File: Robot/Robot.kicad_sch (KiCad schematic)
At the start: 33 parts, among them J1 Barrel_Jack, J10 Conn_01x03_Pin, J11 Stepper_2, J2 Conn_01x02_Pin, J3 Stepper_2, J4 UltraSonic, J5 MotorController, J6 Range, J7 Conn_01x04_Pin, J8 Conn_01x03_Pin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

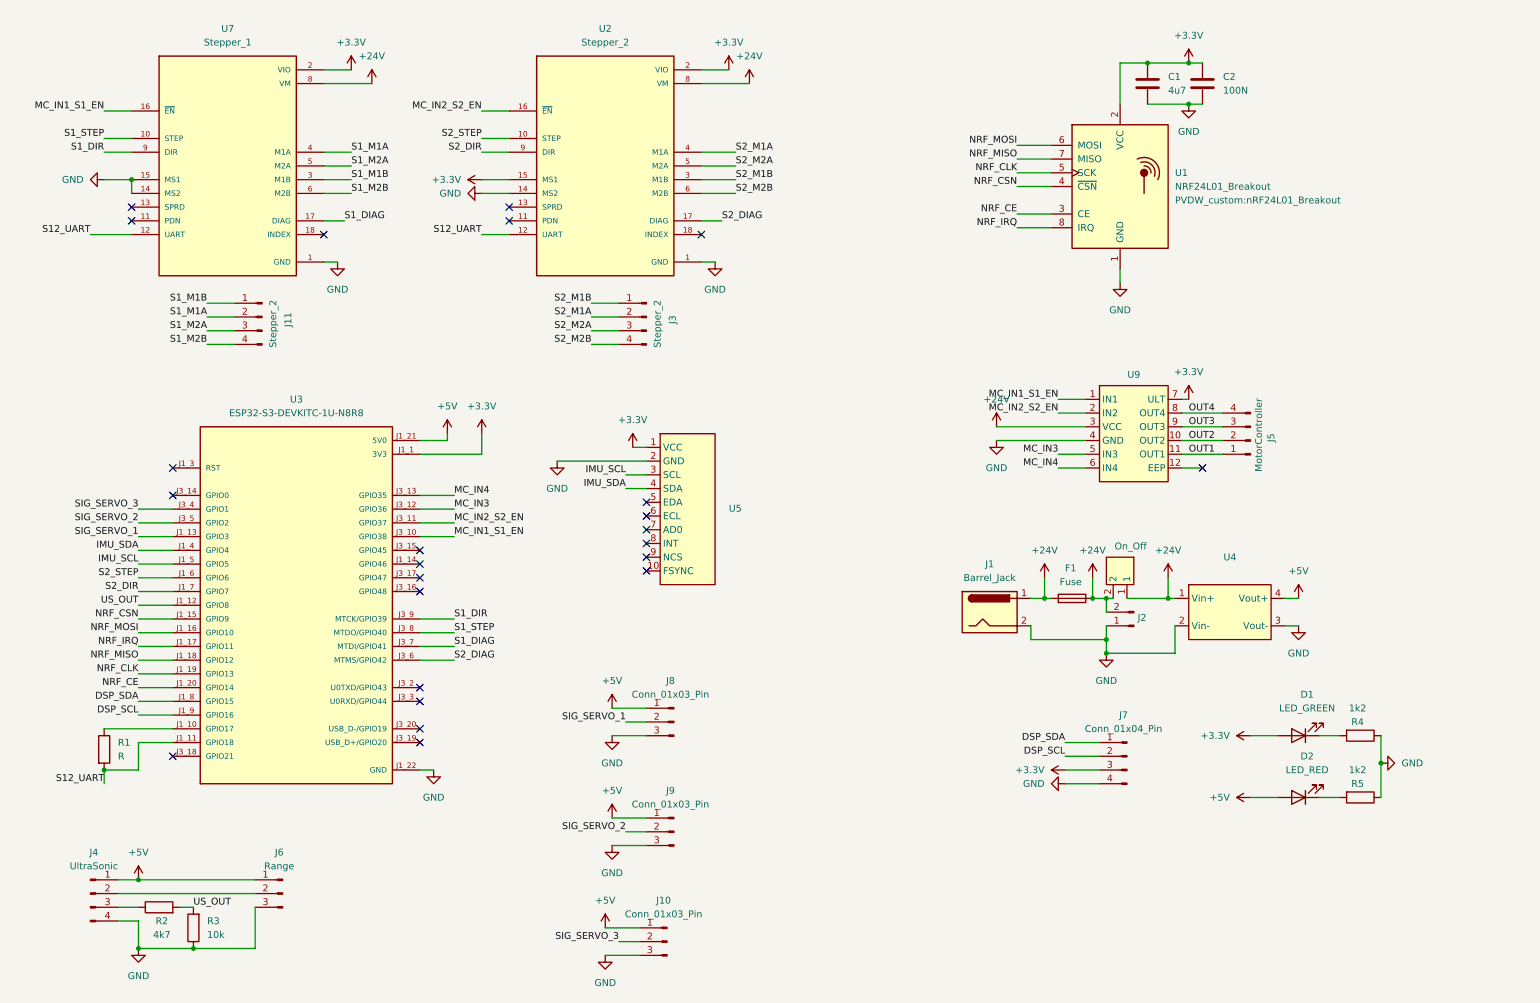
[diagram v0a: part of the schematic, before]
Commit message: Updated robot and created 0402 test pcb
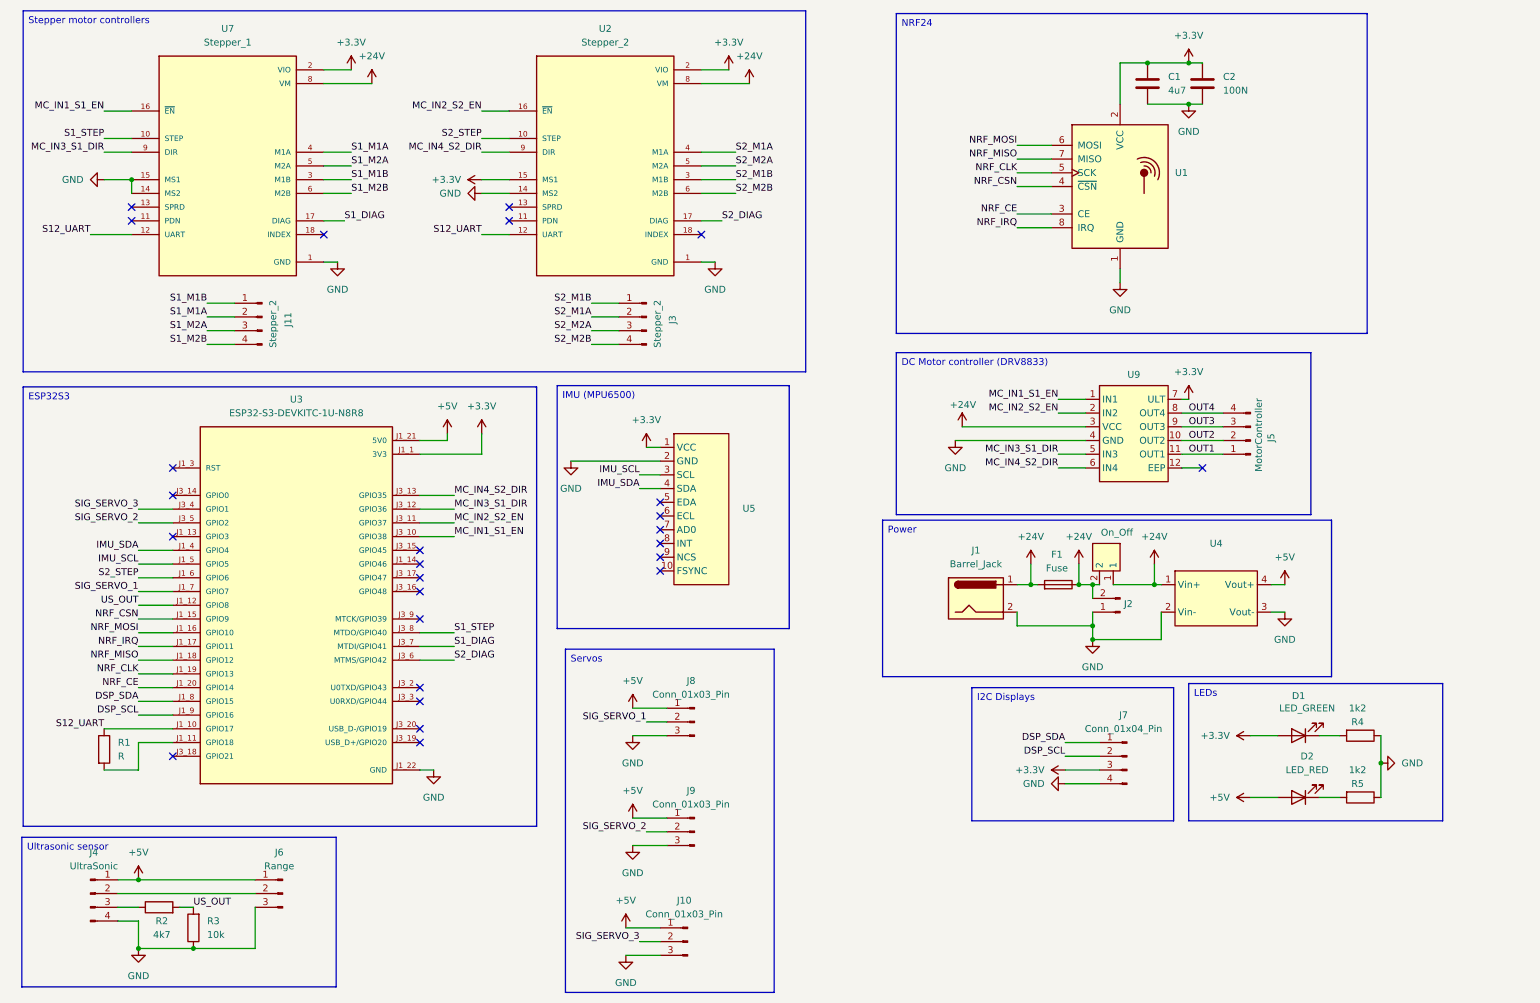
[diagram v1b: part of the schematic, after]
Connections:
- net S12_UART: now also R1.1, U3.J1_10 (GPIO17); no longer R1.2, U3.J1_11 (GPIO18)
- net SIG_SERVO_1: now also U3.J1_7 (GPIO7); no longer U3.J1_13 (GPIO3)
- net MC_IN3 renamed MC_IN3_S1_DIR
- net MC_IN3_S1_DIR: now also U7.9 (DIR)
- net MC_IN4 renamed MC_IN4_S2_DIR
- net MC_IN4_S2_DIR: now also U2.9 (DIR)
- net S1_DIR: no longer names the net of U3.J3_9 (MTCK/GPIO39)
- net S1_DIR: no longer U7.9 (DIR)
- removed net S2_DIR: U2.9 (DIR), U3.J1_7 (GPIO7)
- new net: R1.2, U3.J1_11 (GPIO18)
- no-connect marks 24 -> 26
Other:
- title: (none) -> Self balancing robot
- moved on the sheet: F1, J1, J10, J2, J8, J9, U4, U5

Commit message: New versions for Robot PCBs
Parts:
- removed R2: 4k7, Resistor_SMD:R_0805_2012Metric_Pad1.20x1.40mm_HandSolder, symbol Device:R
- removed R3: 10k, Resistor_SMD:R_0805_2012Metric_Pad1.20x1.40mm_HandSolder, symbol Device:R
- J2, U8: footprint PVDW_custom:Connector_1x2_p2.54_vertical -> PVDW_custom:screw_block_2pin
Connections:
- net +3.3V: now also J4.1 (Pin_1), J6.1 (Pin_1), U9.12 (EEP); no longer U9.7 (ULT)
- net +5V: now also J10.3 (Pin_3), J8.3 (Pin_3), J9.3 (Pin_3); no longer J10.1 (Pin_1), J4.1 (Pin_1), J6.1 (Pin_1), J8.1 (Pin_1), J9.1 (Pin_1)
- net GND: now also J10.1 (Pin_1), J8.1 (Pin_1), J9.1 (Pin_1), U9.3 (GND); no longer J10.3 (Pin_3), J8.3 (Pin_3), J9.3 (Pin_3), U9.4 (GND)
- net S12_UART: now also U2.11 (PDN), U7.11 (PDN); no longer U2.12 (UART), U7.12 (UART)
- net US_OUT: now also J4.3 (Pin_3)
- net UART_TX: now reaches R1.2, U3.J1_11 (GPIO18)
- net IMU_INT: now reaches U5.8 (INT)
- net IMU_INT: now also U3.J1_13 (GPIO3)
- removed net +24V: F1.1, F1.2, J1.1, J2.2 (Pin_2), U2.8 (VM), U4.1 (Vin+), U7.8 (VM), U8.1, U8.2, U9.3 (VCC)
- new net VBat: F1.1, J1.1, J2.2 (Pin_2)
- new net VDC: U2.8 (VM), U4.1 (Vin+), U7.8 (VM), U8.1, U9.4 (VCC)
- new net Vin: F1.2, U8.2
- no-connect marks 26 -> 24
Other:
- moved on the sheet: H1, H2, H3, H4, J2

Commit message: Fixed VCC-GND mixup on drv8833
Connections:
- net GND: now also U9.4 (GND); no longer U9.3 (GND)
- net VDC: now also U9.3 (VCC); no longer U9.4 (VCC)
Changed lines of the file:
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@@
 	(symbol
 		(lib_id "power:GND")
-		(at 187.96 91.44 180)
+		(at 186.69 93.98 0)
 		(unit 1)
 		(exclude_from_sim no)
@@
 		(dnp no)
 		(property "Reference" "#PWR016"
-			(at 187.96 85.09 0)
+			(at 186.69 100.33 0)
 			(effects
 				(font
@@
 		)
 		(property "Value" "GND"
-			(at 187.96 86.36 0)
+			(at 186.69 99.06 0)
 			(effects
 				(font
@@
 		)
 		(property "Footprint" ""
-			(at 187.96 91.44 0)
+			(at 186.69 93.98 0)
 			(effects
 				(font
@@
 		)
 		(property "Datasheet" ""
-			(at 187.96 91.44 0)
+			(at 186.69 93.98 0)
 			(effects
 				(font
@@
 		)
 		(property "Description" "Power symbol creates a global label with name \"GND\" , ground"
-			(at 187.96 91.44 0)
+			(at 186.69 93.98 0)
 			(effects
 				(font
@@
 	(symbol
 		(lib_id "power:+24V")
-		(at 186.69 93.98 180)
+		(at 187.96 91.44 0)
 		(unit 1)
 		(exclude_from_sim no)
@@
 		(dnp no)
 		(property "Reference" "#PWR015"
-			(at 186.69 90.17 0)
+			(at 187.96 95.25 0)
 			(effects
 				(font
@@
 		)
 		(property "Value" "VDC"
-			(at 188.976 98.044 0)
+			(at 185.674 87.376 0)
 			(effects
 				(font
@@
 		)
 		(property "Footprint" ""
-			(at 186.69 93.98 0)
+			(at 187.96 91.44 0)
 			(effects
 				(font
@@
 		)
 		(property "Datasheet" ""
-			(at 186.69 93.98 0)
+			(at 187.96 91.44 0)
 			(effects
 				(font
@@
 		)
 		(property "Description" "Power symbol creates a global label with name \"+24V\""
-			(at 186.69 93.98 0)
-			(effects
-				(font
+			(at 187.96 91.44 0)
+			(effects
+				(font

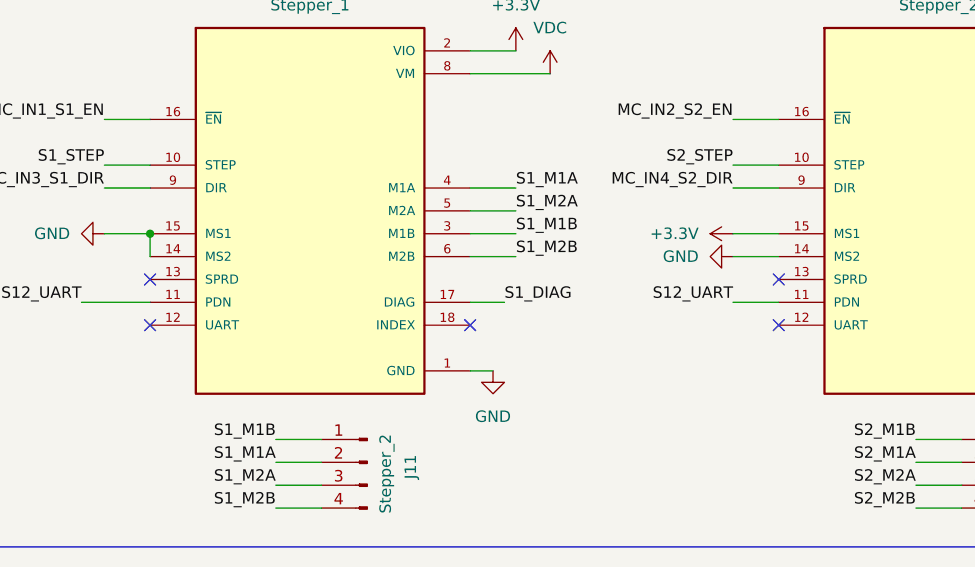
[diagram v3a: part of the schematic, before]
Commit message: Minor bugfixes in Robot PCB (UART connected to the wrong pin of the stepper driver)
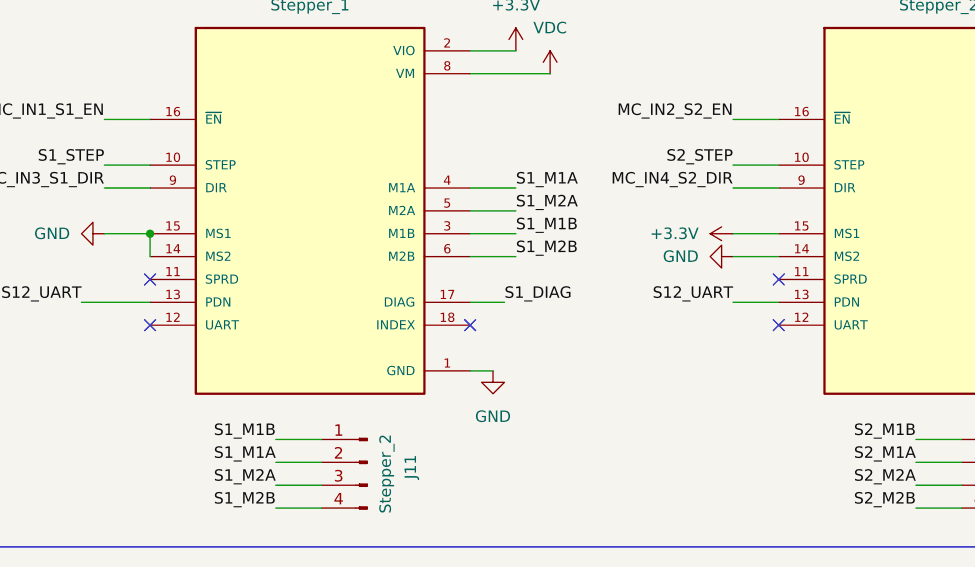
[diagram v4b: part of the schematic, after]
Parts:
- U4, U5, U9: value ~ -> (none)
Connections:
- net S12_UART: now also U2.13 (PDN), U7.13 (PDN); no longer U2.11 (PDN), U7.11 (PDN)

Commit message: New PCB Layout for Robot
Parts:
- removed C1: 4u7, Capacitor_SMD:C_0805_2012Metric_Pad1.18x1.45mm_HandSolder, symbol Device:C
- removed C2: 100N, Capacitor_SMD:C_0805_2012Metric_Pad1.18x1.45mm_HandSolder, symbol Device:C
- removed D1: LED_GREEN, LED_SMD:LED_0805_2012Metric_Pad1.15x1.40mm_HandSolder, symbol Device:LED
- removed D2: LED_RED, LED_SMD:LED_0805_2012Metric_Pad1.15x1.40mm_HandSolder, symbol Device:LED
- removed F1: Fuse, PVDW_custom:FUSE_3544-2, symbol PVDW_custom:Fuse
- removed J1: Barrel_Jack, PVDW_custom:DC_Jack_PCB, symbol PVDW_custom:Barrel_Jack
- removed J10, J8, J9: Conn_01x03_Pin, PVDW_custom:3PIN_SERVO, symbol Connector:Conn_01x03_Pin
- removed J2: Conn_01x02_Pin, PVDW_custom:screw_block_2pin, symbol Connector:Conn_01x02_Pin
- removed J4: UltraSonic, PVDW_custom:Connector_1x4_p2.54_vertical_stepper, symbol PVDW_custom:Conn_01x04_Pin
- removed J5: MotorController, PVDW_custom:Connector_1x4_p2.54_vertical_stepper, symbol PVDW_custom:Conn_01x04_Pin
- removed J6: Range, Connector_PinHeader_2.54mm:PinHeader_1x03_P2.54mm_Vertical, symbol Connector:Conn_01x03_Pin
- removed J7: Conn_01x04_Pin, PVDW_custom:Connector_1x4_p2.54_vertical_stepper, symbol PVDW_custom:Conn_01x04_Pin
- removed R4, R5: 1k2, Resistor_SMD:R_0805_2012Metric_Pad1.20x1.40mm_HandSolder, symbol Device:R
- removed U1: NRF24L01_Breakout, PVDW_custom:nRF24L01_Breakout, symbol PVDW_custom:NRF24L01_Breakout
- removed U8: On_Off, PVDW_custom:screw_block_2pin, symbol PVDW_custom:2Pin_generic
- removed U9: (no value), PVDW_custom:DRV8833, symbol PVDW_custom:drv8833_board
- added J1: Conn_01x02_Pin, Connector_AMASS:AMASS_XT60PW-M_1x02_P7.20mm_Horizontal, symbol Connector:Conn_01x02_Pin
- added J2: Dsp1, PVDW_custom:PinHeader_max7219, symbol Connector:Conn_01x05_Pin
- added J4: Dsp2, PVDW_custom:PinHeader_max7219, symbol Connector:Conn_01x05_Pin
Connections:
- net SIG_SERVO_2 is gone; now on net S2_STEP: U3.J3_5 (GPIO2)
- net +5V: now also J2.1 (Pin_1), J4.1 (Pin_1)
- net GND: now also J1.2 (Pin_2), J2.2 (Pin_2), J4.2 (Pin_2)
- net IMU_INT: now also U3.J1_4 (GPIO4); no longer U3.J1_13 (GPIO3)
- net IMU_SCL: now also U3.J1_6 (GPIO6); no longer U3.J1_5 (GPIO5)
- net IMU_SDA: now also U3.J1_5 (GPIO5); no longer U3.J1_4 (GPIO4)
- net S1_STEP: now also U3.J3_15 (GPIO45); no longer U3.J3_8 (MTDO/GPIO40)
- net S2_DIAG: now also U3.J3_3 (U0RXD/GPIO44); no longer U3.J3_6 (MTMS/GPIO42)
- net S2_STEP: no longer U3.J1_6 (GPIO6)
- net VDC: now also J1.1 (Pin_1)
- net S1_DIR: now reaches U3.J3_16 (GPIO48)
- net S1_DIR: now also U7.9 (DIR)
- net DSP_SCL: no longer names the net of U3.J1_9 (GPIO16)
- net DSP_SDA: no longer names the net of U3.J1_8 (GPIO15)
- net MC_IN1_S1_EN renamed S1_EN
- net MC_IN2_S2_EN: no longer names the net of U3.J3_11 (GPIO37)
- net MC_IN2_S2_EN: no longer U2.16 (~{EN})
- net MC_IN3_S1_DIR: no longer names the net of U3.J3_12 (GPIO36)
- net MC_IN3_S1_DIR: no longer U7.9 (DIR)
- net MC_IN4_S2_DIR: no longer names the net of U3.J3_13 (GPIO35)
- net MC_IN4_S2_DIR: no longer U2.9 (DIR)
- net NRF_CE: no longer names the net of U3.J1_20 (GPIO14)
- net NRF_CLK renamed CS
- net CS: now also J2.4 (Pin_4), J4.4 (Pin_4)
- net NRF_CSN renamed MOSI
- net MOSI: now also J2.3 (Pin_3)
- net NRF_IRQ: no longer names the net of U3.J1_17 (GPIO11)
- net NRF_MISO: no longer names the net of U3.J1_18 (GPIO12)
- net NRF_MOSI renamed CLK
- net CLK: now also J2.5 (Pin_5), J4.5 (Pin_5)
- net SIG_SERVO_1: no longer names the net of U3.J1_7 (GPIO7)
- net SIG_SERVO_3 renamed S2_EN
- net S2_EN: now also U2.16 (~{EN})
- new net S2_DIR: U2.9 (DIR), U3.J3_6 (MTMS/GPIO42)
- no-connect marks 24 -> 28

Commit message: New version
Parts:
- removed J4: Dsp2, PVDW_custom:PinHeader_max7219, symbol Connector:Conn_01x05_Pin
- removed U4: (no value), PVDW_custom:LM1584EN, symbol PVDW_custom:LM1584EN
- added C1, C2: C_Polarized, Capacitor_THT:C_Radial_D10.0mm_H20.0mm_P5.00mm, symbol Device:C_Polarized
- added J4: Conn_01x02_Pin, Connector_PinHeader_2.54mm:PinHeader_1x02_P2.54mm_Vertical, symbol Connector:Conn_01x02_Pin
- added U1: LM7805_TO220, Package_TO_SOT_THT:TO-220-3_Vertical, symbol Regulator_Linear:LM7805_TO220
- J1: footprint Connector_AMASS:AMASS_XT60PW-M_1x02_P7.20mm_Horizontal -> Connector_AMASS:AMASS_XT60-F_1x02_P7.20mm_Vertical
- J2: footprint PVDW_custom:PinHeader_max7219 -> Connector_PinHeader_2.54mm:PinHeader_1x05_P2.54mm_Vertical
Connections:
- net +5V: now also C1.1, U1.3 (VO)
- net GND: now also J1.1 (Pin_1), C1.2, C2.2, J4.2 (Pin_2), U1.2 (GND); no longer J1.2 (Pin_2)
- net IMU_INT: now also U3.J3_12 (GPIO36); no longer U3.J1_4 (GPIO4)
- net IMU_SCL: now also U3.J3_14 (GPIO0); no longer U3.J1_6 (GPIO6)
- net IMU_SDA: now also U3.J3_13 (GPIO35); no longer U3.J1_5 (GPIO5)
- net VDC: now also J1.2 (Pin_2), C2.1, U1.1 (VI); no longer J1.1 (Pin_1)
- net OTA: now reaches U3.J1_14 (GPIO46)
- net OTA: now also J4.1 (Pin_1)
- no-connect marks 28 -> 24
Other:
- moved on the sheet: J1

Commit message: New version
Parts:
- added J5: Conn_01x05_Pin, Connector_PinHeader_2.54mm:PinHeader_1x05_P2.54mm_Vertical, symbol Connector:Conn_01x05_Pin
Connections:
- net +3.3V: now also J5.1 (Pin_1)
- net GND: now also J5.2 (Pin_2)
- net GPIO5: now reaches U3.J1_5 (GPIO5)
- net GPIO5: now also J5.3 (Pin_3)
- net GPIO6: now reaches U3.J1_6 (GPIO6)
- net GPIO6: now also J5.4 (Pin_4)
- net GPIO7: now reaches U3.J1_7 (GPIO7)
- net GPIO7: now also J5.5 (Pin_5)
- net US_OUT: no longer names the net of U3.J1_12 (GPIO8)
- no-connect marks 24 -> 28
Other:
- moved on the sheet: J2

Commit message: Ordered version
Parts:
- added J6: Conn_01x02_Pin, Connector_PinHeader_2.54mm:PinHeader_1x02_P2.54mm_Vertical, symbol Connector:Conn_01x02_Pin
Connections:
- net VDC: now also J6.2 (Pin_2); no longer J1.2 (Pin_2)
- new net VBAT: J1.2 (Pin_2), J6.1 (Pin_1)
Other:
- moved on the sheet: J1
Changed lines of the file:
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@@
 	)
 	(junction
+		(at 189.23 120.65)
+		(diameter 0)
+		(color 0 0 0 0)
+	)
+	(junction
 		(at 34.29 45.72)
 		(diameter 0)
@@
 	(wire
 		(pts
-			(xy 200.66 123.19) (xy 208.28 123.19)
-		)
-		(stroke
-			(width 0)
-			(type default)
-		)
-	)
-	(wire
-		(pts
 			(xy 35.56 154.94) (xy 29.21 154.94)
 		)
@@
 	(wire
 		(pts
+			(xy 189.23 120.65) (xy 193.04 120.65)
+		)
+		(stroke
+			(width 0)
+			(type default)
+		)
+	)
+	(wire
+		(pts
 			(xy 35.56 119.38) (xy 41.91 119.38)
 		)
@@
 	(wire
 		(pts
-			(xy 200.66 120.65) (xy 208.28 120.65)
+			(xy 34.29 45.72) (xy 34.29 48.26)
 		)
 		(stroke
@@
 	(wire
 		(pts
-			(xy 34.29 45.72) (xy 34.29 48.26)
+			(xy 189.23 116.84) (xy 189.23 120.65)
 		)
 		(stroke
@@
 	(wire
 		(pts
+			(xy 189.23 123.19) (xy 208.28 123.19)
+		)
+		(stroke
+			(width 0)
+			(type default)
+		)
+	)
+	(wire
+		(pts
 			(xy 179.07 77.47) (xy 182.88 77.47)
 		)
@@
 	(wire
 		(pts
+			(xy 195.58 120.65) (xy 208.28 120.65)
+		)
+		(stroke
+			(width 0)
+			(type default)
+		)
+	)
+	(wire
+		(pts
 			(xy 115.57 97.79) (xy 132.08 97.79)
 		)
@@
 		)
 	)
+	(label "VBAT"
+		(at 189.23 116.84 90)
+		(effects
+			(font
+				(size 1.27 1.27)
+			)
+			(justify left bottom)
+		)
+	)
 	(label "IMU_SCL"
 		(at 35.56 104.14 180)
@@
 	(symbol
 		(lib_id "Connector:Conn_01x02_Pin")
-		(at 195.58 123.19 0)
+		(at 184.15 123.19 0)
 		(mirror x)
 		(unit 1)
@@
 		(dnp no)
 		(property "Reference" "J1"
-			(at 196.215 128.27 0)
+			(at 184.785 128.27 0)
 			(show_name no)
 			(do_not_autoplace no)
@@
 		)
 		(property "Value" "Conn_01x02_Pin"
-			(at 196.215 125.73 0)
+			(at 184.785 125.73 0)
 			(show_name no)
 			(do_not_autoplace no)
@@
 		)
 		(property "Footprint" "Connector_AMASS:AMASS_XT60-F_1x02_P7.20mm_Vertical"
-			(at 195.58 123.19 0)
+			(at 184.15 123.19 0)
 			(hide yes)
 			(show_name no)
@@
 		)
 		(property "Datasheet" ""
-			(at 195.58 123.19 0)
+			(at 184.15 123.19 0)
 			(hide yes)
 			(show_name no)
@@
 		)
 		(property "Description" "Generic connector, single row, 01x02, script generated"
-			(at 195.58 123.19 0)
+			(at 184.15 123.19 0)
 			(hide yes)
 			(show_name no)
@@
 					(unit 1)
 				)
+			)
+		)
+	)
+	(symbol
+		(lib_id "Connector:Conn_01x02_Pin")
+		(at 193.04 115.57 90)
+		(mirror x)
+		(unit 1)
+		(body_style 1)
+		(exclude_from_sim no)
+		(in_bom yes)
+		(on_board yes)
+		(in_pos_files yes)
+		(dnp no)
+		(fields_autoplaced yes)
+		(property "Reference" "J6"
+			(at 196.85 114.9349 90)
+			(show_name no)
+			(do_not_autoplace no)
+			(effects
+				(font
+					(size 1.27 1.27)
+				)
+				(justify right)
+			)
+		)
+		(property "Value" "Conn_01x02_Pin"
+			(at 196.85 117.4749 90)
+			(show_name no)
+			(do_not_autoplace no)
+			(effects
+				(font
+					(size 1.27 1.27)
+				)
+				(justify right)
+			)
+		)
+		(property "Footprint" "Connector_PinHeader_2.54mm:PinHeader_1x02_P2.54mm_Vertical"
+			(at 193.04 115.57 0)
+			(hide yes)
+			(show_name no)
+			(do_not_autoplace no)
+			(effects
+				(font
+					(size 1.27 1.27)
+				)
+			)
+		)
+		(property "Datasheet" ""
+			(at 193.04 115.57 0)
+			(hide yes)
+			(show_name no)
+			(do_not_autoplace no)
+			(effects
+				(font
+					(size 1.27 1.27)
+				)
+			)
+		)
+		(property "Description" "Generic connector, single row, 01x02, script generated"
+			(at 193.04 115.57 0)
+			(hide yes)
+			(show_name no)
+			(do_not_autoplace no)
+			(effects
+				(font
+					(size 1.27 1.27)
+				)
+			)
+		)
+		(pin "2"
+		)
+		(pin "1"
+		)
+		(instances
+			(project "Robot"
+				(path "/1cd93e02-a9ab-4d45-b65e-b2e72610ab46"
+					(reference "J6")
+					(unit 1)
+				)
